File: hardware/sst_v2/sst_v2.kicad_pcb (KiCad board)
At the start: 4 copper layers, 60 x 90 mm, 96 parts, among them U1 Pico_2_W, U2 ADS131M04IPWR, U3 DS3231SN, Y1 ECS-2520MVLC-081.92-BN-TR

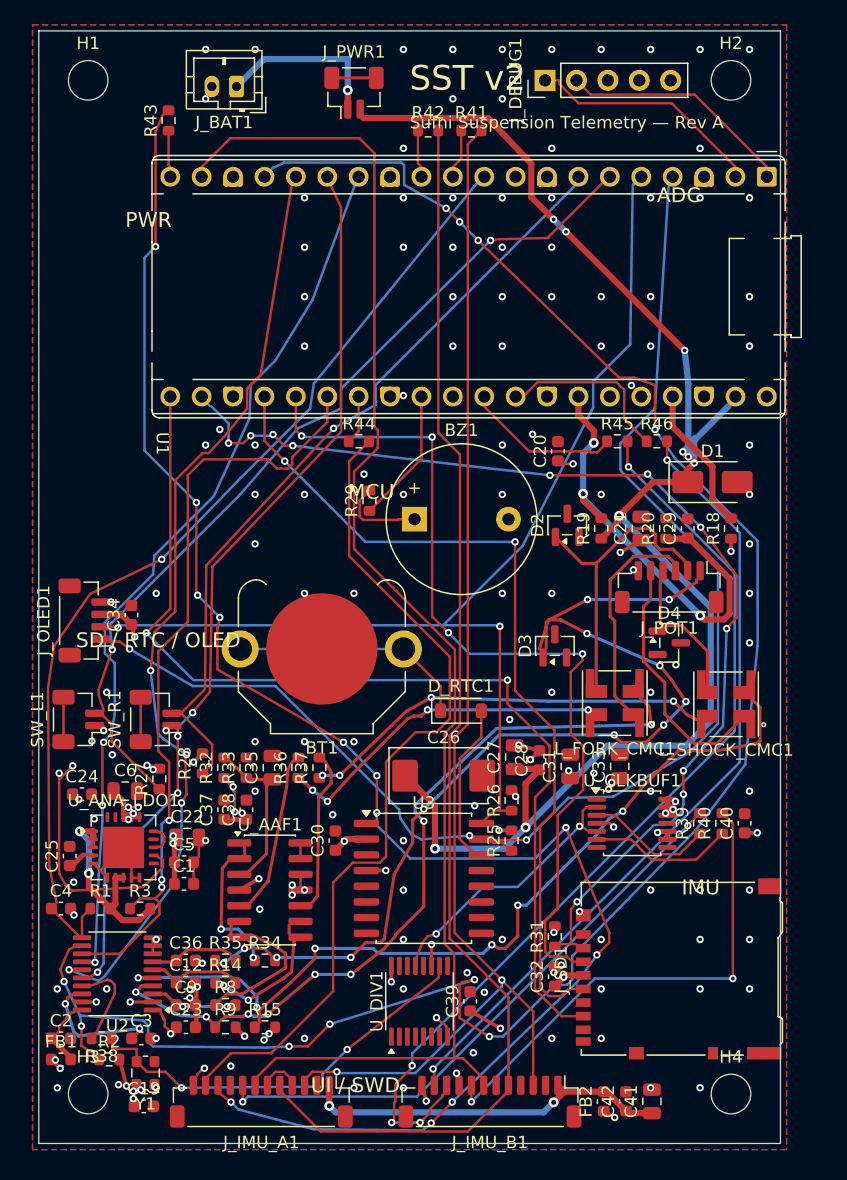
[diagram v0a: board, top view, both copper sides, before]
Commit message: hw: Rev. 3 Review — LDO-Pinbelegung, VSYS-Diode, Verpolschutz, Fertigungsdaten
Fehler behoben:
- TPS7A4700: Symbol nach SBVS204G (GND-Pin lag an 3,3 V, OUT/IN vertauscht,
  ANY-OUT an 3,3 V), Footprint Texas RGW0020A, LDO-Bereich neu geroutet,
  Eingangs-C 10 uF (C22), Ausgangs-C 22 uF (C6)
- USB-VBUS speiste in den LiPo: Schottky D_VSYS1 zwischen +VBAT_SW und VSYS
- RTC-Backup-Diode verpolt: entfernt, CR1220 direkt an VBAT
- Buzzer-Footprint auf 5-mm-Raster (TDK PS1240P02BT)
- R18 an 3V3_EN entfernt, DS3231-RST offen
- ADS131M04 DVDD aus +3V3_DIG über FB1 (Logikpegel 3,3 V)
- CMC nach Murata-Ersatzschaltbild beschaltet (Gleichtaktdämpfung)
- J_DEBUG1 als 1x3 UART (SWD-Pins waren unverbunden)
- DRC: Lötstopp-Steg 0,1 mm, Kupfer-Kante 0,3 mm, J_SD1-Schirm-Pads gekürzt,
  volle Anbindung der GND-Pads

Empfehlungen umgesetzt: Verpolschutz Q_RP1 (DMG2305UX), Polymer-Tantal C26,
1 uF direkt an AVDD, 100 nF an 74HC4040 (C44), microSD-DAT1-Pull-up (R48),
Montagelöcher im Schaltplan, Silkscreen bereinigt.

ERC 0 Fehler, DRC 0 Fehler/0 offene Verbindungen/0 Paritätsfehler.
Gerber, Bohrdaten, BOM und CPL neu erzeugt. README für Rev. 3 neu.

Co-Authored-By: Claude Opus 5.5 <noreply@anthropic.com>
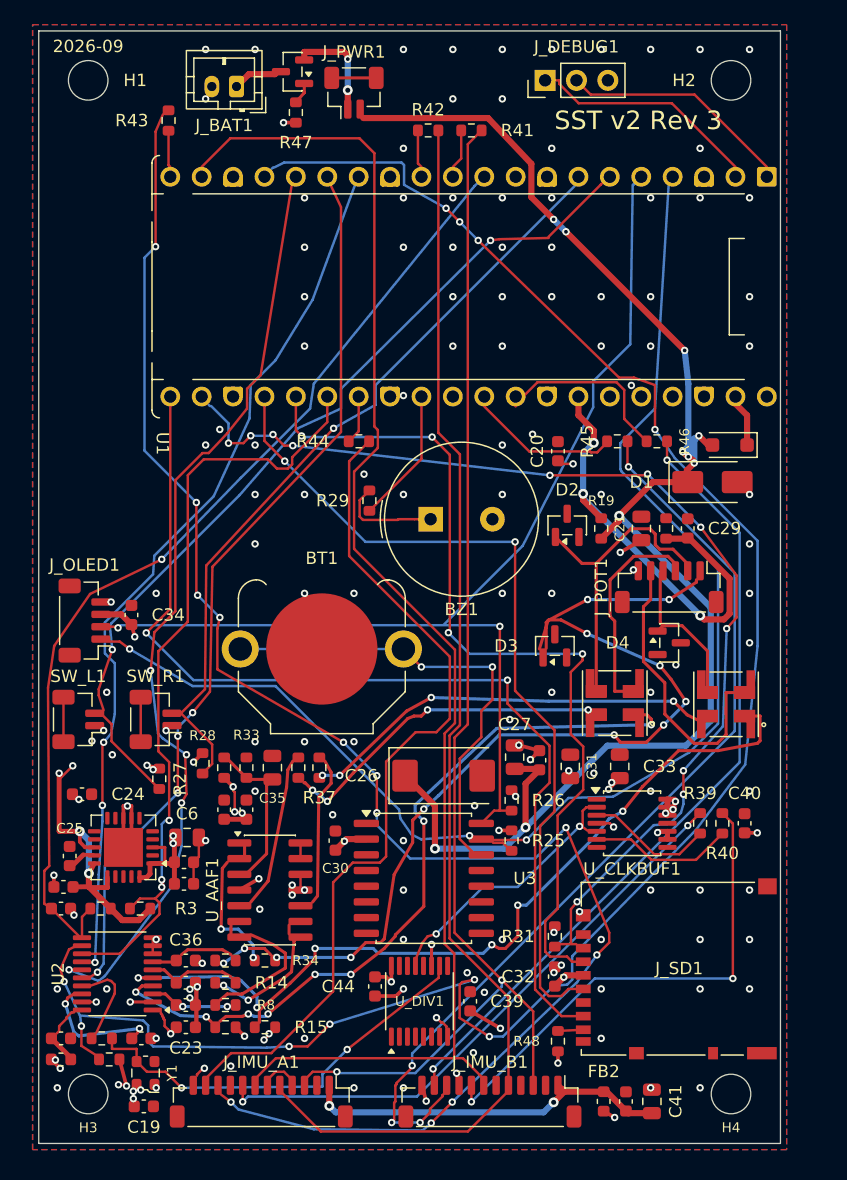
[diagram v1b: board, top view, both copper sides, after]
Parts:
- removed D_RTC1: 1N4148, Diode_SMD:D_SOD-123
- removed R18: 10k, Resistor_SMD:R_0603_1608Metric
- added C44: 100nF X7R, Capacitor_SMD:C_0603_1608Metric, F.Cu at (111.7, 125.3)
- added D_VSYS1: PMEG3020EH, Diode_SMD:D_SOD-123F, F.Cu at (140.4, 81.5)
- added Q_RP1: DMG2305UX, Package_TO_SOT_SMD:SOT-23, F.Cu at (105.0, 51.3)
- added R47: 10k, Resistor_SMD:R_0603_1608Metric, F.Cu at (105.3, 54.6)
- added R48: 47k, Resistor_SMD:R_0603_1608Metric, F.Cu at (126.5, 129.7)
- BZ1: footprint Buzzer_Beeper:Buzzer_12x9.5RM7.6 -> Buzzer_Beeper:Buzzer_TDK_PS1240P02BT_D12.2mm_H6.5mm
- C1: value 1uF X7R -> 100nF X7R
- C22: value 10uF X7R -> 10uF X5R; footprint Capacitor_SMD:C_0805_2012Metric -> Capacitor_SMD:C_0603_1608Metric
- C23: value 100nF X7R -> 1uF X7R
- C26: value 100uF/10V Tant -> 100uF 10V Polymer
- C6: value 10uF X7R -> 22uF X7R
- J_DEBUG1: value SWD+UART Header 1x5 -> UART Header 1x3; footprint Connector_PinHeader_2.54mm:PinHeader_1x05_P2.54mm_Vertical -> Connector_PinHeader_2.54mm:PinHeader_1x03_P2.54mm_Vertical
- U_ANA_LDO1: footprint Package_DFN_QFN:QFN-20-1EP_5x5mm_P0.65mm_EP3.35x3.35mm -> Package_DFN_QFN:Texas_RGW0020A_VQFN-20-1EP_5x5mm_P0.65mm_EP3.15x3.15mm
- moved C22 10.8 mm to (86.5, 117.2), turned to 180 degrees
- moved C6 6.25 mm to (96.5, 113.2)
- moved BZ1 1.30 mm to (116.2, 87.5)
- turned U_ANA_LDO1 to 180 degrees
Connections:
- BT1 pad 1: RTC_BAT_RAW -> RTC_VBAT
- C22 pad 1: +3V0_ANA -> +3V3_DIG
- FB1 pad 1: +3V0_ANA -> +3V3_DIG
- J_BAT1 pad 1: +VBAT -> VBAT_IN
- J_DEBUG1 pad 3: SWCLK -> GND
- J_SD1 pad 8: SD_NC2 -> SD_DAT1
- L_FORK_CMC1 pad 1: J_FORK_POT_GND -> FORK_POT_GND_F
- L_FORK_CMC1 pad 2: FORK_POT_GND_F -> J_FORK_POT_GND
- L_SHOCK_CMC1 pad 1: J_SHOCK_POT_GND -> SHOCK_POT_GND_F
- L_SHOCK_CMC1 pad 2: SHOCK_POT_GND_F -> J_SHOCK_POT_GND
- U1 pad 37: +3V3_EN -> unconnected-(U1-3V3_EN-Pad37)
- U1 pad 39: +VBAT_SW -> VSYS
- U3 pad 4: +3V3_DIG -> unconnected-(U3-RST-Pad4)
- U_ANA_LDO1 pad 1: +3V3_DIG -> +3V0_ANA
- U_ANA_LDO1 pad 10: GND -> unconnected-(U_ANA_LDO1-0P4V-Pad10)
- U_ANA_LDO1 pad 11: GND -> unconnected-(U_ANA_LDO1-0P2V-Pad11)
- U_ANA_LDO1 pad 12: +3V3_DIG -> unconnected-(U_ANA_LDO1-0P1V-Pad12)
- U_ANA_LDO1 pad 13: +3V0_ANA_FB -> +3V3_DIG
- U_ANA_LDO1 pad 14: GND -> LDO_NRSS
- U_ANA_LDO1 pad 15: +3V0_ANA_FB -> +3V3_DIG
- U_ANA_LDO1 pad 16: +3V0_ANA -> +3V3_DIG
- U_ANA_LDO1 pad 17: +3V0_ANA -> unconnected-(U_ANA_LDO1-NC-Pad17)
- U_ANA_LDO1 pad 18: +3V0_ANA -> unconnected-(U_ANA_LDO1-NC-Pad18)
- U_ANA_LDO1 pad 19: (no net) -> unconnected-(U_ANA_LDO1-NC-Pad19)
- U_ANA_LDO1 pad 2: +3V3_DIG -> unconnected-(U_ANA_LDO1-NC-Pad2)
- U_ANA_LDO1 pad 20: (no net) -> +3V0_ANA
- U_ANA_LDO1 pad 3: +3V3_DIG -> +3V0_ANA
- U_ANA_LDO1 pad 4: LDO_NRSS -> unconnected-(U_ANA_LDO1-6P4V2-Pad4)
- U_ANA_LDO1 pad 5: GND -> unconnected-(U_ANA_LDO1-6P4V1-Pad5)
- U_ANA_LDO1 pad 6: GND -> unconnected-(U_ANA_LDO1-3P2V-Pad6)
- U_ANA_LDO1 pad 7: +3V3_DIG -> GND
- U_ANA_LDO1 pad 8: +3V3_DIG -> GND
- U_ANA_LDO1 pad 9: GND -> unconnected-(U_ANA_LDO1-0P8V-Pad9)
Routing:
- net RTC_VBAT: track 13.4 -> 38.3 mm, vias 0 -> 2
- net RTC_BAT_RAW: track 19.4 -> 0.00 mm
- net +3V3_DIG: track 73.9 -> 62.5 mm, vias 35 -> 36
- net +3V3_EN: track 11.0 -> 0.00 mm
- net +VBAT: track 14.0 -> 8.62 mm, vias 1 -> 2
- net VSYS: track 0.00 -> 4.31 mm
- net VBAT_IN: track 0.00 -> 4.07 mm
- net J_SHOCK_POT_GND: track 20.9 -> 23.7 mm
- net SD_DAT1: track 0.00 -> 2.05 mm
- net +VBAT_SW: track 123.2 -> 121.2 mm, vias 9 -> 10
- net +3V0_ANA_FB: track 1.85 -> 0.00 mm
- net Q_RP_G: track 0.00 -> 1.78 mm
- net +3V0_ANA: track 20.9 -> 19.5 mm, vias 14 -> 8
- net BUZ_DRV_A_S: track 7.02 -> 8.32 mm
- net J_FORK_POT_GND: track 18.6 -> 17.6 mm
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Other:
- rule solder_mask_min_width: 0.25 -> 0.1
- board text added: "2026-09"
- board text added: "SST v2 Rev 3"
- board text removed: "ADC"
- board text removed: "IMU"
- board text removed: "MCU"
- board text removed: "PWR"
- board text removed: "SD / RTC / OLED"
- board text removed: "SST v2"
- board text removed: "Sufni Suspension Telemetry — Rev A"
- board text removed: "UI / SWD"

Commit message: hw: Umplatzierung, Nacharbeit und Lader MCP73831
Umplatzierung:
- Pico 2 mm nach links, USB-Buchse innerhalb der Platine
- Poti-Eingang links, OLED/Taster rechts, Analogblock 2 mm nach rechts
- R49 (47k) an SD_DAT2, Y1-3D-Modell SG210

Nacharbeit:
- J_SD1 innerhalb der Kante und weg von H4
- BT1 und BZ1 getauscht, Einschubweg der Zelle frei
- C3 1,9 mm an U2 CAP, C40 2,7 mm an U_CLKBUF1 VCC
- Freiraum >= 3,5 mm um H3/H4

Lader:
- MCP73831 unter dem Pico, 300 mA, STAT-Teiler an GP6 (CHG_STAT)
- sst_v2.kicad_dru erlaubt Courtyard-Ueberdeckung mit U1 nur fuer die Lader-Teile

Digitalnetze neu geroutet (Freerouting, Sperrflaeche ueber Analogblock).
ERC 0 Fehler, DRC 0 Fehler / 0 offene Verbindungen.
Fertigungsdaten, BOM/CPL (102 Positionen) und README aktualisiert.

Co-Authored-By: Claude Opus 5.5 <noreply@anthropic.com>
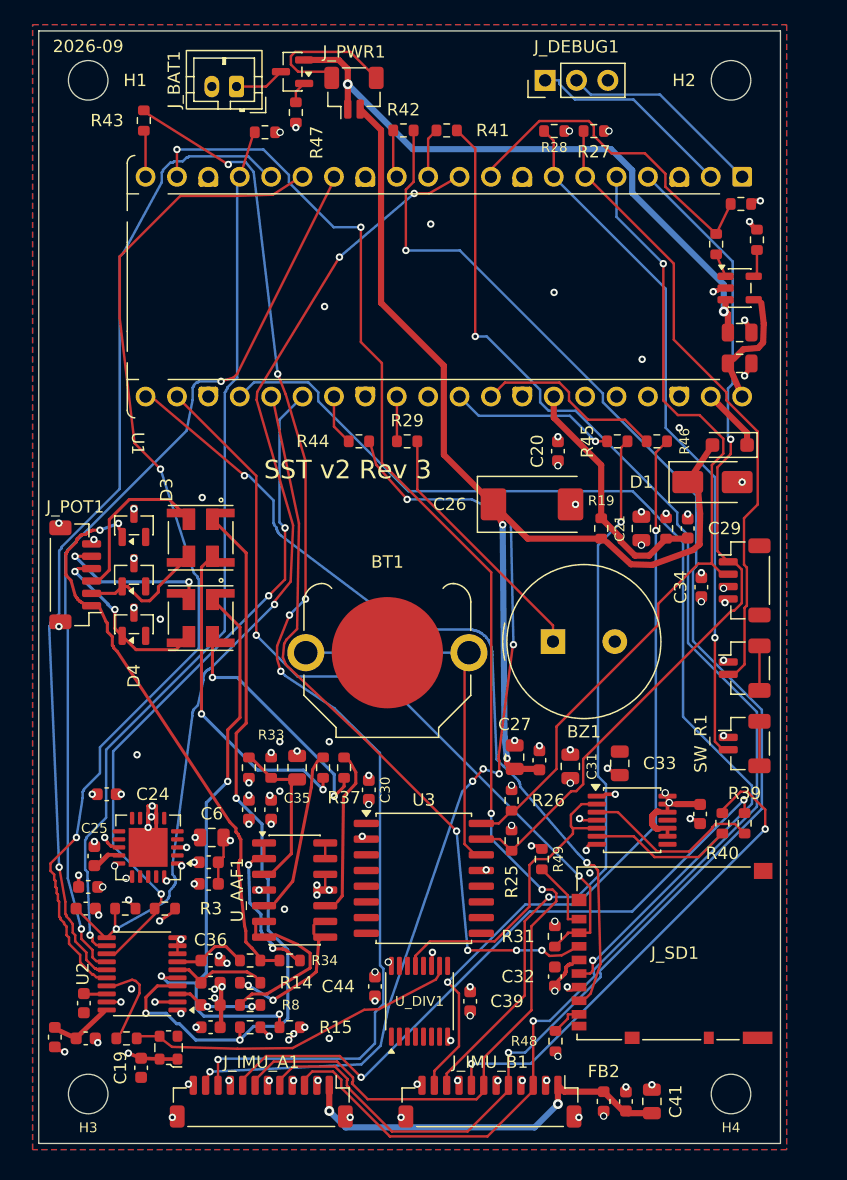
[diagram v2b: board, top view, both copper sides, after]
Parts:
- added C_CHG1: 4.7uF X5R, Capacitor_SMD:C_0805_2012Metric, F.Cu at (141.2, 74.9)
- added C_CHG2: 4.7uF X5R, Capacitor_SMD:C_0805_2012Metric, F.Cu at (141.2, 72.4)
- added R49: 47k, Resistor_SMD:R_0603_1608Metric, F.Cu at (125.2, 115.0)
- added R_PROG: 3.3k 1%, Resistor_SMD:R_0603_1608Metric, F.Cu at (142.6, 64.9)
- added R_STAT1: 10k, Resistor_SMD:R_0603_1608Metric, F.Cu at (139.3, 65.2)
- added R_STAT2: 20k, Resistor_SMD:R_0603_1608Metric, F.Cu at (141.3, 62.0)
- added U_CHG1: MCP73831T-2ACI/OT, Package_TO_SOT_SMD:SOT-23-5, F.Cu at (141.2, 68.8)
- moved R2 76.1 mm to (102.8, 56.2)
- moved R27 63.1 mm to (129.4, 56.1), turned to 0 degrees
- moved R28 58.5 mm to (126.2, 56.1), turned to 0 degrees
- moved SW_L1 54.1 mm to (141.6, 99.5), turned to -90 degrees
- moved J_OLED1 53.5 mm to (141.6, 92.5), turned to -90 degrees
- moved J_POT1 48.1 mm to (87.5, 92.0), turned to 90 degrees
- moved SW_R1 47.7 mm to (141.6, 105.7), turned to -90 degrees
- moved C34 46.2 mm to (138.1, 93.0)
- moved D4 43.3 mm to (92.2, 96.0), turned to 90 degrees
- moved L_SHOCK_CMC1 43.1 mm to (97.6, 95.5), turned to -90 degrees
- moved L_FORK_CMC1 36.1 mm to (97.6, 89.0), turned to -90 degrees
- moved D3 35.4 mm to (92.2, 88.0)
- moved D2 35.3 mm to (92.2, 92.0)
- moved C26 23.1 mm to (124.4, 86.3)
- moved BZ1 14.0 mm to (126.1, 97.4)
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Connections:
- U1 pad 9: GP6_RSV -> CHG_STAT
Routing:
- net ADC_CS: track 156.0 -> 69.5 mm, vias 10 -> 1
- net +VBAT: track 8.62 -> 50.3 mm
- net POT_EXC: track 81.9 -> 43.3 mm, vias 12 -> 2
- net +3V3_DIG: track 62.5 -> 24.1 mm, vias 36 -> 31
- net +VBAT_SW: track 121.2 -> 84.5 mm, vias 10 -> 2
- net DISP_SDA: track 106.4 -> 70.1 mm, vias 3 -> 1
- net IMU_CS0: track 133.4 -> 101.8 mm, vias 12 -> 6
- net CHG_STAT: track 0.00 -> 27.9 mm
- net IMU_MOSI: track 102.4 -> 125.3 mm, vias 0 -> 2
- net DISP_SCL: track 91.2 -> 68.3 mm, vias 2 -> 1
- net SD_CS: track 86.4 -> 64.5 mm, vias 11 -> 2
- net SHOCK_POT_GND_F: track 68.9 -> 48.0 mm, vias 6 -> 3
- net IMU_SCLK: track 100.9 -> 121.3 mm
- net BTN_L: track 71.0 -> 51.4 mm, vias 2 -> 0
- net SD_SCK: track 68.3 -> 85.8 mm, vias 2 -> 1
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
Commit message: hw: Platinenbeschriftung SSDAQ v2 Rev 3 an den linken Rand
Co-Authored-By: Claude Fable 5.1 <noreply@anthropic.com>
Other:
- board text added: "SSDAQ v2 Rev 3"
- board text removed: "SST v2 Rev 3"
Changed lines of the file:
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@@
 		)
 	)
-	(gr_text "SST v2 Rev 3"
-		(at 109.5 83.5 0)
+	(gr_text "SSDAQ v2 Rev 3"
+		(at 88 68.5 90)
 		(layer "F.SilkS")
 		(effects

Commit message: hw: Layout — Fertigungsregeln, Antennen-Sperrflaeche, Abblockung, R50
- 23 Vias +3V3_DIG 0,7/0,4 mm (Restring 0,15), Silkscreen 0,15 mm / 1,0 mm
- min_via_annular_width und min_text_thickness 0,15
- Rule Area Pico-Antenne: alle Kupferlagen, keine Bahnen/Vias/Pours,
  volle Pico-Breite + 1 mm; ADC_CS/SCK/SDI/SDO neu geroutet
- C1 an U_AAF1 Pin 4, C_CHG1 an U_CHG1 Pin 4 (C_CHG1/C_CHG2 getauscht)
- R50 unter dem Pico an Pin 10, FID1-FID3, Titelblock Rev. 3
- Zonen gefuellt; DRC 0 Fehler, 0 offen, 0 Paritaet

Co-Authored-By: Claude Opus 5.5 <noreply@anthropic.com>
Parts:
- added FID1: Fiducial, Fiducial:Fiducial_1mm_Mask3mm, F.Cu at (135.9, 54.8)
- added FID2: Fiducial, Fiducial:Fiducial_1mm_Mask3mm, F.Cu at (89.5, 106.8)
- added FID3: Fiducial, Fiducial:Fiducial_1mm_Mask3mm, F.Cu at (136.9, 101.3)
- added R50: 100, Resistor_SMD:R_0603_1608Metric, F.Cu at (116.6, 62.3)
- R_STAT2: value 20k -> 15k
- moved C1 2.78 mm to (100.7, 118.3), turned to -90 degrees
- moved C_CHG1 2.50 mm to (141.2, 72.4), turned to 180 degrees
- moved C_CHG2 2.50 mm to (141.2, 74.9)
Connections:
- net +3V0_DVDD renamed +3V3_DVDD
- U1 pad 10: ADC_RST -> ADC_RST_MCU
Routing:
- net ADC_SDI: track 82.9 -> 91.9 mm, vias 2 -> 3
- net ADC_SDO: track 78.3 -> 84.6 mm, vias 1 -> 2
- net +VBAT: track 50.3 -> 53.7 mm
- net ADC_RST_MCU: track 0.00 -> 2.85 mm
- net ADC_RST: track 79.9 -> 78.2 mm
- net +3V0_ANA: track 5.55 -> 7.16 mm, vias 13 -> 12
- net ADC_CS: track 69.5 -> 70.8 mm, vias 1 -> 3
- net POT_EXC: track 43.3 -> 44.6 mm
- net ADC_SCK: track 72.5 -> 73.3 mm
- net GND: track 50.1 -> 50.4 mm, vias 95 -> 96

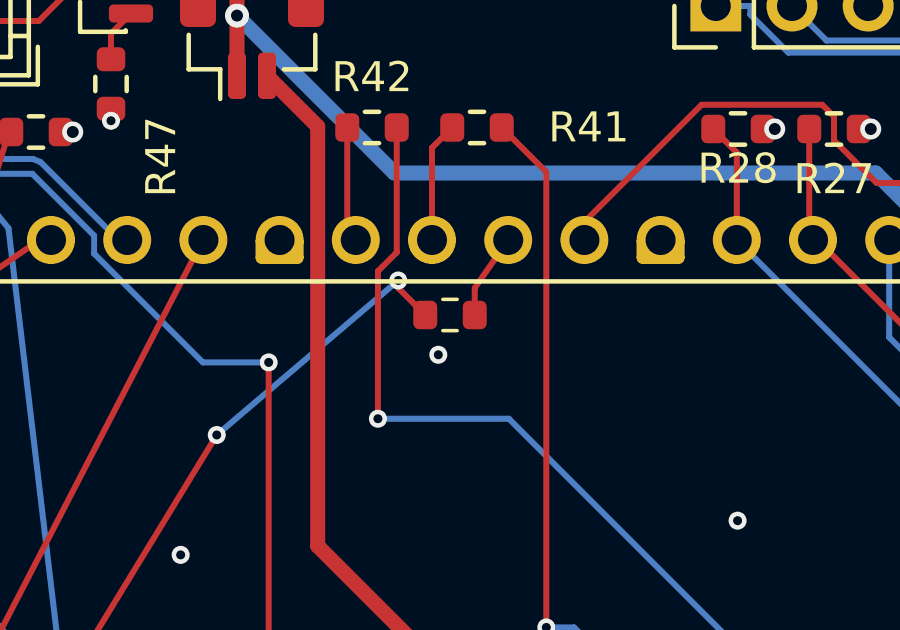
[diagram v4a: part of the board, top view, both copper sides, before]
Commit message: hw: R_STAT2 10k (CHG_STAT max. 2,6 V), R50-Silkscreen 0,15 mm, Fertigungsdaten neu
Co-Authored-By: Claude Fable 5.1 <noreply@anthropic.com>
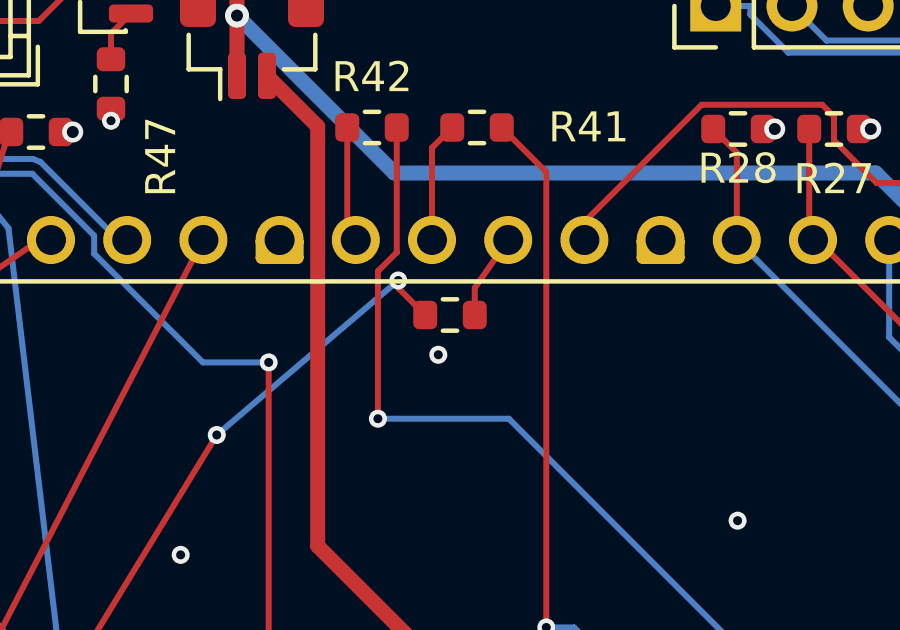
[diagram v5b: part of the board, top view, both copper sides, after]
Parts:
- R_STAT2: value 15k -> 10k
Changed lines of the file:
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@@
 			)
 		)
-		(property "Value" "15k"
+		(property "Value" "10k"
 			(at 0 1.43 0)
 			(layer "F.Fab")
@@
 			(end 0.237258 0.5225)
 			(stroke
-				(width 0.12)
+				(width 0.15)
 				(type solid)
 			)
@@
 			(end 0.237258 -0.5225)
 			(stroke
-				(width 0.12)
+				(width 0.15)
 				(type solid)
 			)
